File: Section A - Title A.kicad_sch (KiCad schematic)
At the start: 0 parts

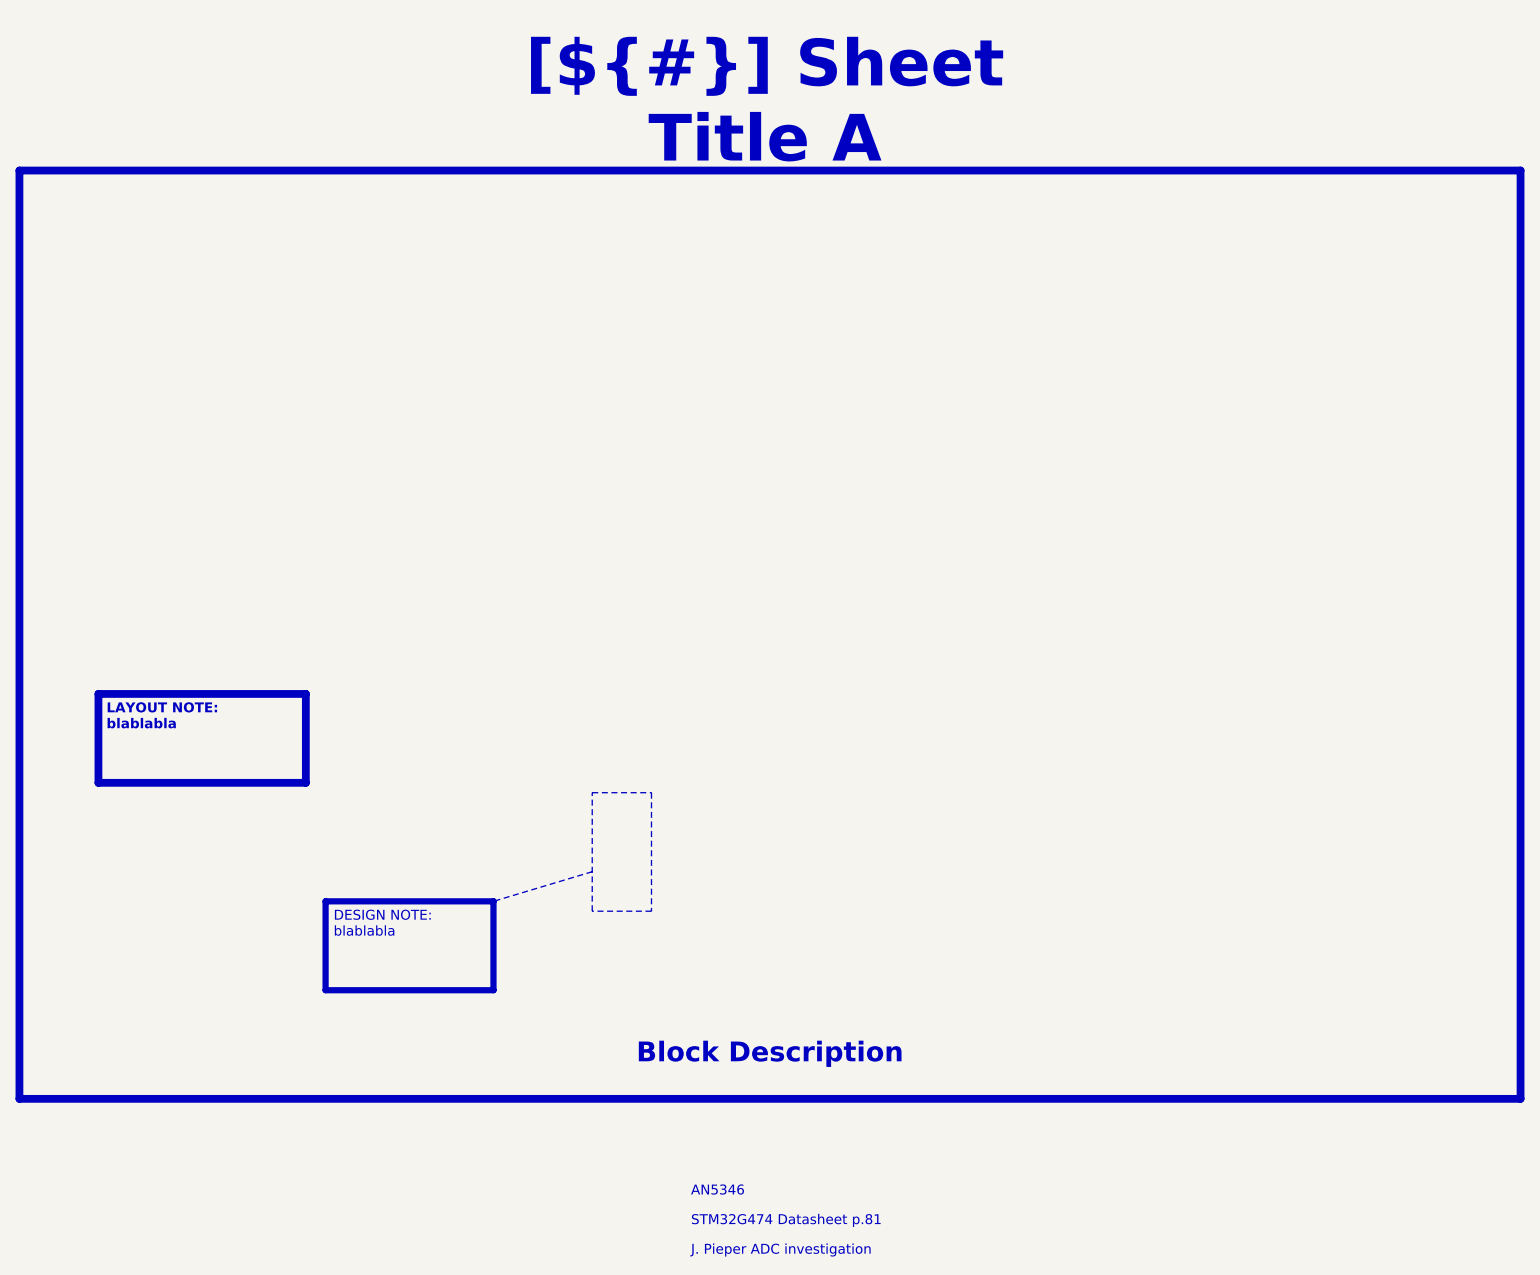
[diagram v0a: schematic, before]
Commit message: customise for 2 layer
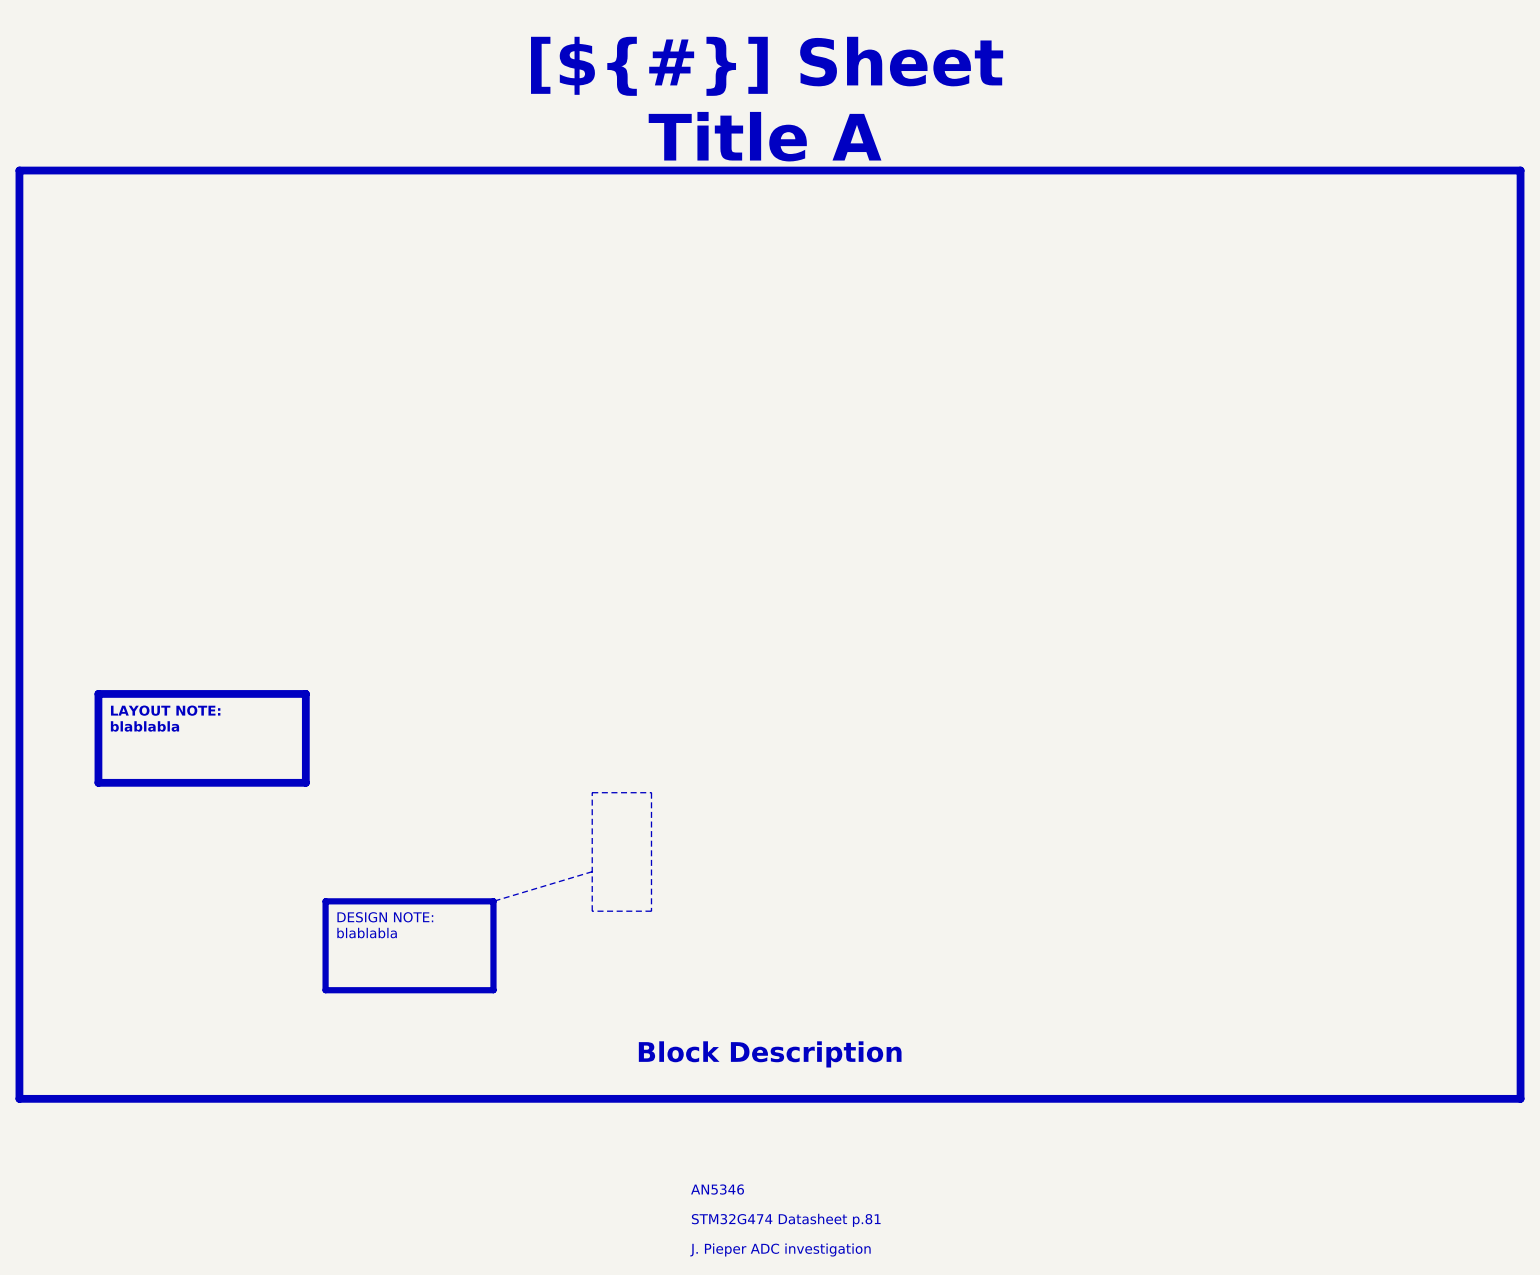
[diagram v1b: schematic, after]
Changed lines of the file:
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@@
 (kicad_sch
-	(version 20231120)
+	(version 20250114)
 	(generator "eeschema")
-	(generator_version "8.0")
+	(generator_version "9.0")
 	(paper "A4")
 	(title_block
@@
 		(rev "${REVISION}")
 		(company "${COMPANY}")
-	)
-	(polyline
-		(pts
-			(xy 129.54 120.65) (xy 116.84 124.46)
-		)
-		(stroke
-			(width 0)
-			(type dot)
-			(color 255 0 0 1)
-		)
 	)
 	(rectangle
@@
 		(fill
 			(type none)
-		)
-	)
-	(text_box "LAYOUT NOTE:\nblablabla"
-		(exclude_from_sim no)
-		(at 66.04 97.79 0)
-		(size 26.67 11.43)
-		(stroke
-			(width 1)
-			(type solid)
-			(color 0 0 255 1)
-		)
-		(fill
-			(type none)
-		)
-		(effects
-			(font
-				(face "Arial")
-				(size 1.27 1.27)
-				(thickness 0.4)
-				(bold yes)
-				(color 0 0 255 1)
-			)
-			(justify left top)
-		)
-	)
-	(text_box "[${#}] ${TITLE}"
-		(exclude_from_sim no)
-		(at 115.57 15.24 0)
-		(size 72.39 12.7)
-		(stroke
-			(width -0.0001)
-			(type default)
-		)
-		(fill
-			(type none)
-		)
-		(effects
-			(font
-				(face "Times New Roman")
-				(size 6 6)
-				(thickness 1.2)
-				(bold yes)
-				(color 162 22 34 1)
-			)
-		)
-	)
-	(text_box "Block Description"
-		(exclude_from_sim no)
-		(at 57.15 139.7 0)
-		(size 190.5 7.62)
-		(stroke
-			(width -0.0001)
-			(type default)
-		)
-		(fill
-			(type none)
-		)
-		(effects
-			(font
-				(face "Times New Roman")
-				(size 2.54 2.54)
-				(thickness 0.508)
-				(bold yes)
-				(color 162 22 34 1)
-			)
-			(justify bottom)
-		)
-	)
-	(text_box "DESIGN NOTE:\nblablabla"
-		(exclude_from_sim no)
-		(at 95.25 124.46 0)
-		(size 21.59 11.43)
-		(stroke
-			(width 0.8)
-			(type solid)
-			(color 250 236 0 1)
-		)
-		(fill
-			(type none)
-		)
-		(effects
-			(font
-				(face "Arial")
-				(size 1.27 1.27)
-				(color 0 0 0 1)
-			)
-			(justify left top)
 		)
 	)
@@
 		)
 	)
+	(text_box "LAYOUT NOTE:\nblablabla"
+		(exclude_from_sim no)
+		(at 66.04 97.79 0)
+		(size 26.67 11.43)
+		(margins 1.4525 1.4525 1.4525 1.4525)
+		(stroke
+			(width 1)
+			(type solid)
+			(color 0 0 255 1)
+		)
+		(fill
+			(type none)
+		)
+		(effects
+			(font
+				(face "Arial")
+				(size 1.27 1.27)
+				(thickness 0.4)
+				(bold yes)
+				(color 0 0 255 1)
+			)
+			(justify left top)
+		)
+	)
+	(text_box "[${#}] ${TITLE}"
+		(exclude_from_sim no)
+		(at 115.57 15.24 0)
+		(size 72.39 12.7)
+		(margins 4.4999 4.4999 4.4999 4.4999)
+		(stroke
+			(width -0.0001)
+			(type default)
+		)
+		(fill
+			(type none)
+		)
+		(effects
+			(font
+				(face "Times New Roman")
+				(size 6 6)
+				(thickness 1.2)
+				(bold yes)
+				(color 162 22 34 1)
+			)
+		)
+	)
+	(text_box "Block Description"
+		(exclude_from_sim no)
+		(at 57.15 139.7 0)
+		(size 190.5 7.62)
+		(margins 1.9049 1.9049 1.9049 1.9049)
+		(stroke
+			(width -0.0001)
+			(type default)
+		)
+		(fill
+			(type none)
+		)
+		(effects
+			(font
+				(face "Times New Roman")
+				(size 2.54 2.54)
+				(thickness 0.508)
+				(bold yes)
+				(color 162 22 34 1)
+			)
+			(justify bottom)
+		)
+	)
+	(text_box "DESIGN NOTE:\nblablabla"
+		(exclude_from_sim no)
+		(at 95.25 124.46 0)
+		(size 21.59 11.43)
+		(margins 1.3525 1.3525 1.3525 1.3525)
+		(stroke
+			(width 0.8)
+			(type solid)
+			(color 250 236 0 1)
+		)
+		(fill
+			(type none)
+		)
+		(effects
+			(font
+				(face "Arial")
+				(size 1.27 1.27)
+				(color 0 0 0 1)
+			)
+			(justify left top)
+		)
+	)
+	(polyline
+		(pts
+			(xy 129.54 120.65) (xy 116.84 124.46)
+		)
+		(stroke
+			(width 0)
+			(type dot)
+			(color 255 0 0 1)
+		)
+	)
